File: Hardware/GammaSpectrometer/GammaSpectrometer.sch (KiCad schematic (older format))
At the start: 0 parts

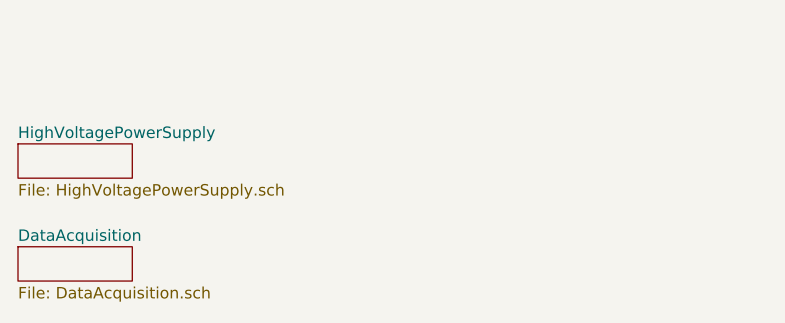
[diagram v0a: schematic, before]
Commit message: Remove old version of simulation. In KiCad model added draft of HV stabilizer.
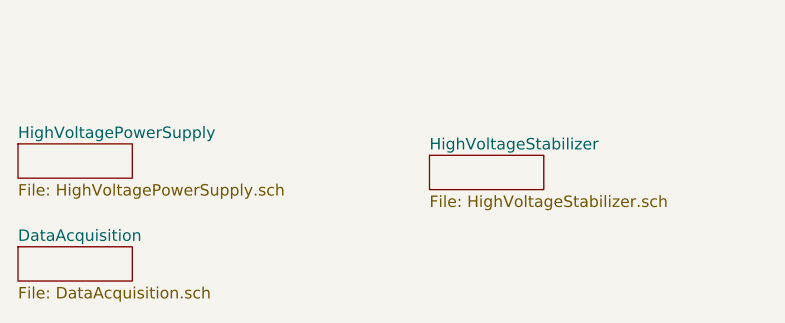
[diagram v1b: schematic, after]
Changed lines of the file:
@@
 $Descr A4 11693 8268
 encoding utf-8
-Sheet 1 3
+Sheet 1 4
 Title ""
 Date ""
@@
 F1 "DataAcquisition.sch" 50
 $EndSheet
+$Sheet
+S 5450 3800 500  150
+U 5FDE08B1
+F0 "HighVoltageStabilizer" 50
+F1 "HighVoltageStabilizer.sch" 50
+$EndSheet
 $EndSCHEMATC

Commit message: draft of component placement on PCB
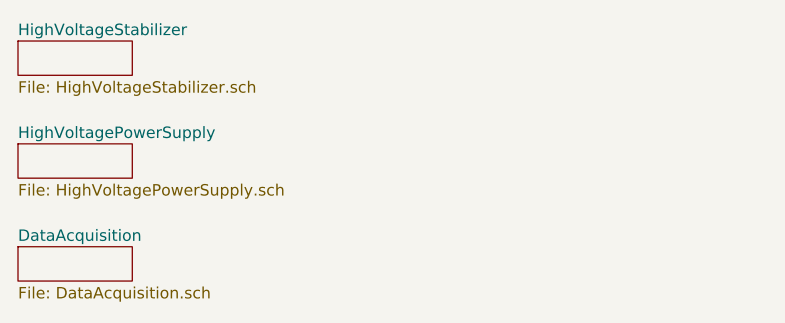
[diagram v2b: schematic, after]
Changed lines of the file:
@@
 $EndSheet
 $Sheet
-S 5450 3800 500  150
+S 3650 3300 500  150
 U 5FDE08B1
 F0 "HighVoltageStabilizer" 50
